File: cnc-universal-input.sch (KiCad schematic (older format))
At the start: 143 parts, among them J1 3PT, J10 2PT, J12 USB_B_Mini, J13 2PT, J14 2PT, J15 2PT, J16 2PT, J17 2PT, J18 2PT, J2 3PT, J3 3PT, J4 3PT, J5 3PT, J6 3PT, J7 3PT, J8 3PT, J9 AVR-ISP-6, Q1 2N7002, Q11 2N7002, Q12 2N7002, Q13 2N7002, Q2 2N7002, Q3 2N7002, Q4 2N7002, Q5 2N7002, Q6 2N7002, Q7 2N7002, Q8 2N7002, Q9 2N7002, SW1 RESET, SW2 BTN, U1 ATmega328PB-AU, U10 EL357NC, U11 EL357NC, U12 EL357NC, U13 EL357NC, U14 EL357NC, U15 EL357NC, U16 EL357NC, U18 CH340G, U19 XL1509-5E1, U2 74HC595, U3 74HC595, U4 74HC595, U5 4051, U6 XL1509-12E1, U7 ADuM1201AR, U8 SGMOP07CXS8G/TR, U9 EL357NC, Y1 16MHz, Y2 12MHz

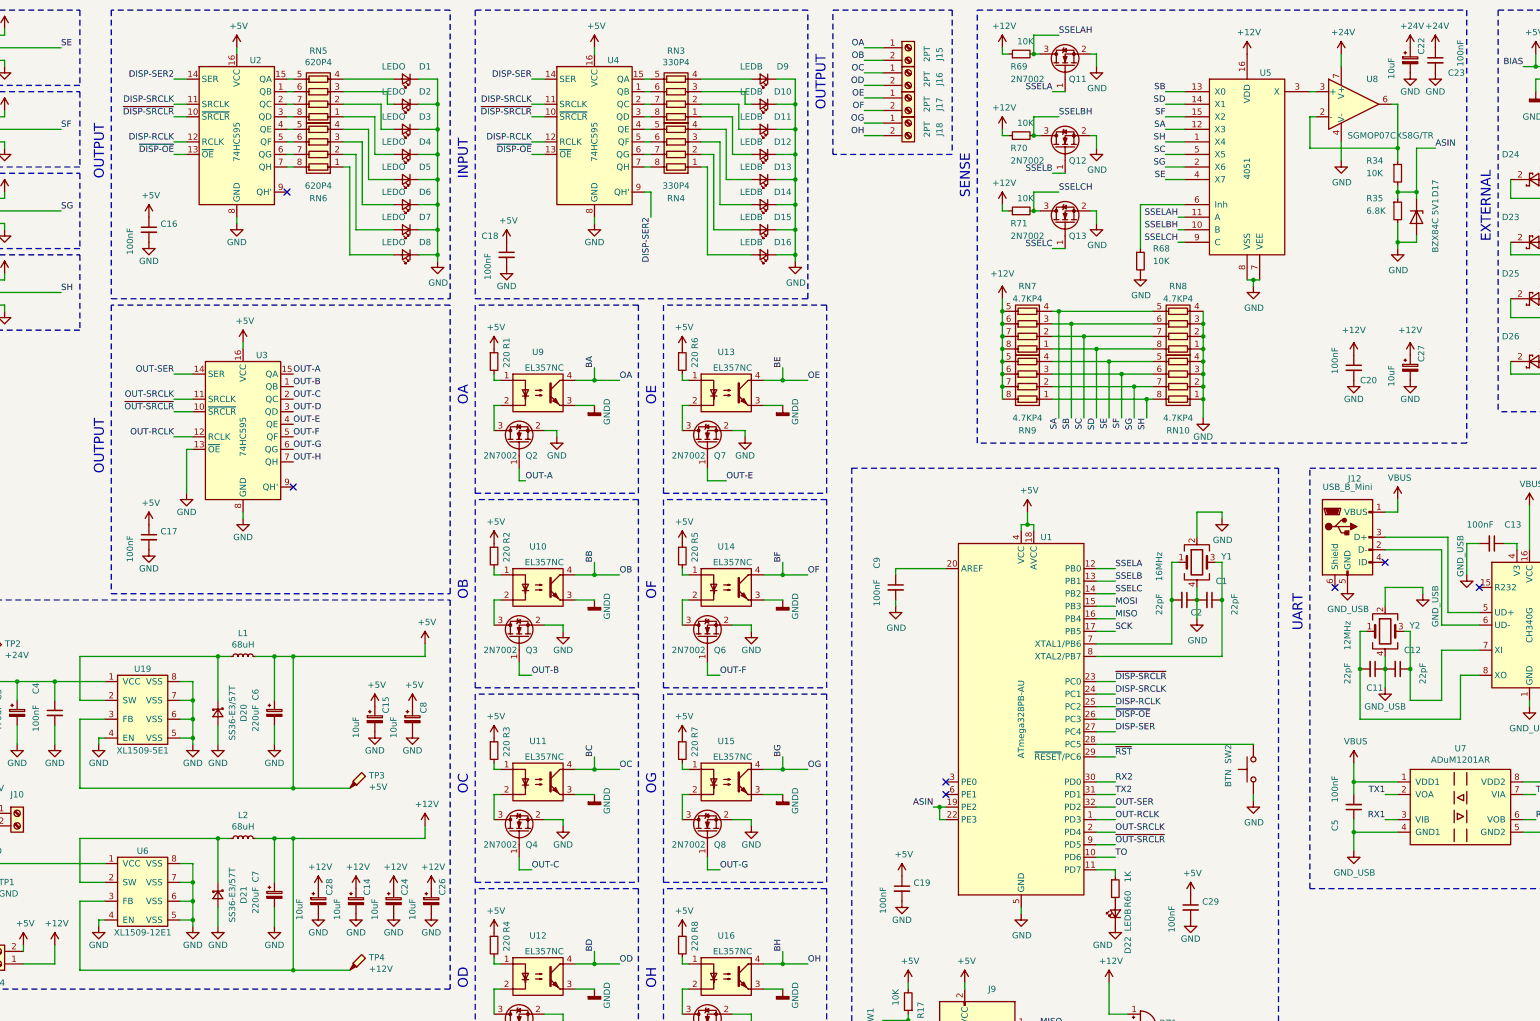
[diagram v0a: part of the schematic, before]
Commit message: Keep something in stock ffs...
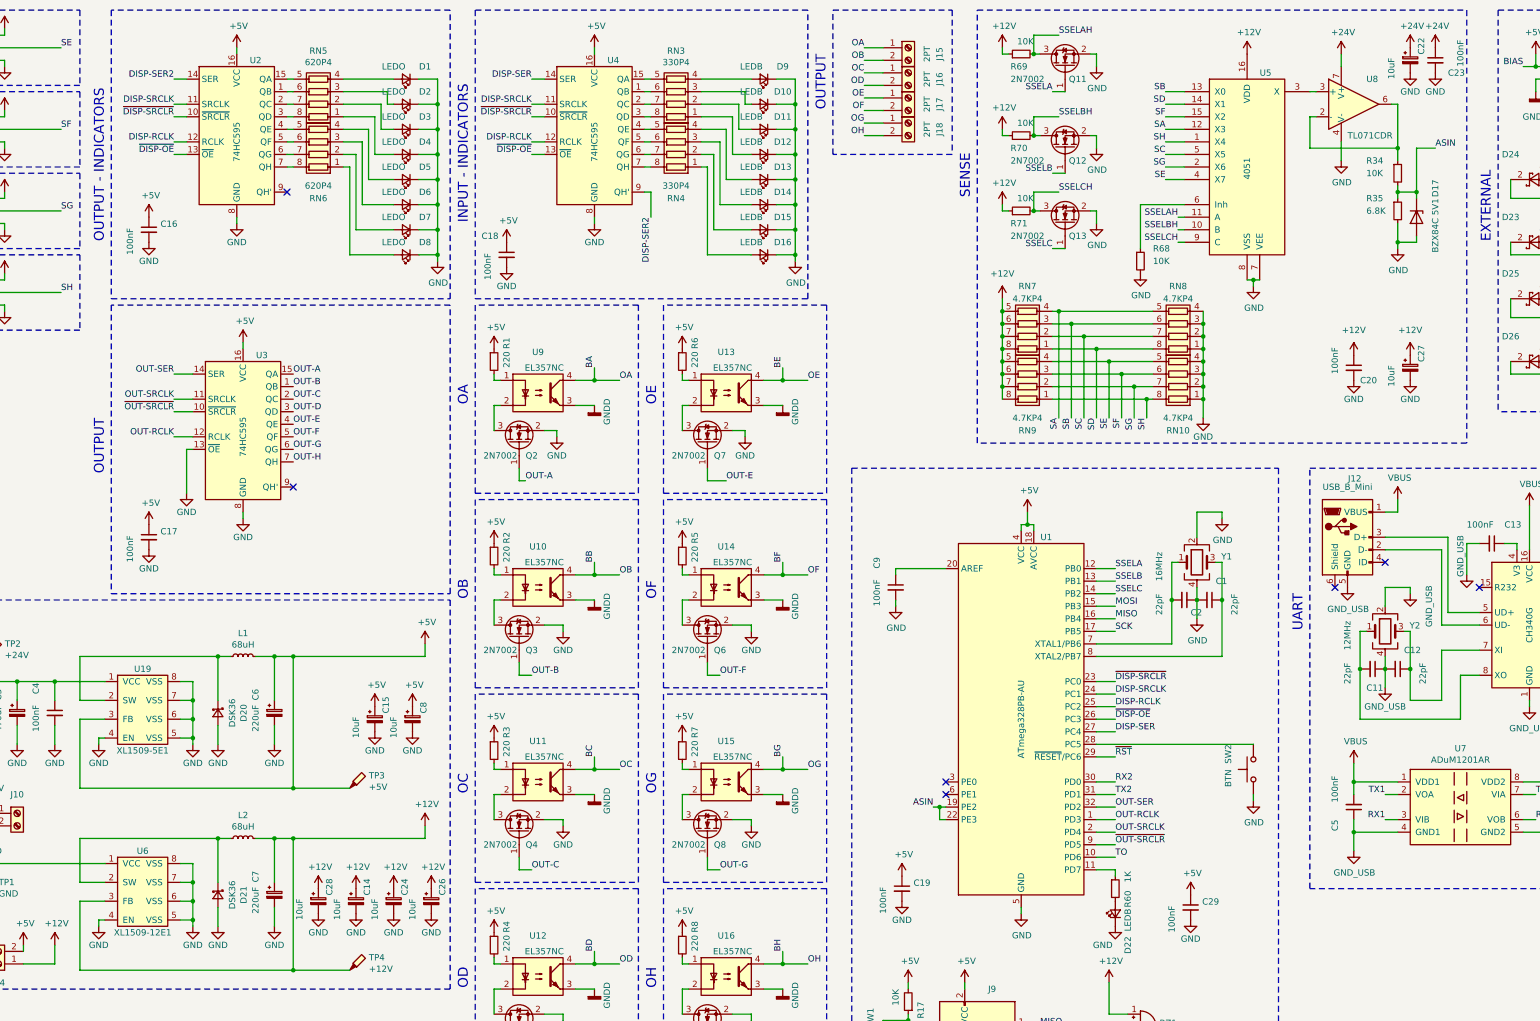
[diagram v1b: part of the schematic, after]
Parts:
- D20, D21: value SS36-E3/57T -> DSK36; footprint Diode_SMD:D_2114_3652Metric -> Diode_SMD:D_SOD-123F; LCSC C35722 -> C106913
- U10, U11, U12, U13, U14, U15, U16, U9: footprint IvyBit-footprints:SOP-4_4.1x4.4x2.54P -> Package_SO:SO-4_4.4x3.9mm_P2.54mm
- U8: value SGMOP07CXS8G/TR -> TL071CDR; LCSC C89712 -> C14449
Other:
- note added: "INPUT - INDICATORS"
- note added: "OUTPUT - INDICATORS"
- note removed: "INPUT"
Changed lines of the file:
@@
 P 13200 1300
 F 0 "U8" H 13300 1500 50  0000 L CNN
-F 1 "SGMOP07CXS8G/TR" H 13150 1050 50  0000 L CNN
+F 1 "TL071CDR" H 13150 1050 50  0000 L CNN
 F 2 "Package_SO:SOIC-8_3.9x4.9mm_P1.27mm" H 13100 1100 50  0001 L CNN
 F 3 "https://datasheet.lcsc.com/lcsc/2004131003_SGMICRO-SGMOP07CXS8G-TR_C89712.pdf" H 13350 1450 50  0001 C CNN
-F 4 "C89712" H 13200 1300 50  0001 C CNN "LCSC"
+F 4 "C14449" H 13200 1300 50  0001 C CNN "LCSC"
 	1    13200 1300
 	1    0    0    -1
@@
 Wire Notes Line
 	8850 550  6200 550
-Text Notes 6150 1900 1    79   ~ 0
-INPUT
+Text Notes 6150 2250 1    79   ~ 0
+INPUT - INDICATORS
 $Comp
 L cnc-universal-input-rescue:LED_Small-Device D1
@@
 Wire Notes Line
 	6000 550  3300 550
-Text Notes 3250 1900 1    79   ~ 0
-OUTPUT
+Text Notes 3250 2400 1    79   ~ 0
+OUTPUT - INDICATORS
 Text Label 11300 5000 0    50   ~ 0
 SSELA
@@
 F 0 "U9" H 6700 3925 50  0000 C CNN
 F 1 "EL357NC" H 6750 3800 50  0000 C CNN
-F 2 "IvyBit-footprints:SOP-4_4.1x4.4x2.54P" H 6500 3400 50  0001 L CIN
+F 2 "Package_SO:SO-4_4.4x3.9mm_P2.54mm" H 6500 3400 50  0001 L CIN
 F 3 "https://datasheet.lcsc.com/lcsc/1810271030_Everlight-Elec-EL357N-C-TA-G_C29981.pdf" H 6700 3600 50  0001 L CNN
 F 4 "C29981" H 6700 3600 50  0001 C CNN "LCSC"
@@
 F 0 "U10" H 6700 5475 50  0000 C CNN
 F 1 "EL357NC" H 6750 5350 50  0000 C CNN
-F 2 "IvyBit-footprints:SOP-4_4.1x4.4x2.54P" H 6500 4950 50  0001 L CIN
+F 2 "Package_SO:SO-4_4.4x3.9mm_P2.54mm" H 6500 4950 50  0001 L CIN
 F 3 "https://datasheet.lcsc.com/lcsc/1810271030_Everlight-Elec-EL357N-C-TA-G_C29981.pdf" H 6700 5150 50  0001 L CNN
 F 4 "C29981" H 6700 5150 50  0001 C CNN "LCSC"
@@
 F 0 "U13" H 8200 3925 50  0000 C CNN
 F 1 "EL357NC" H 8250 3800 50  0000 C CNN
-F 2 "IvyBit-footprints:SOP-4_4.1x4.4x2.54P" H 8000 3400 50  0001 L CIN
+F 2 "Package_SO:SO-4_4.4x3.9mm_P2.54mm" H 8000 3400 50  0001 L CIN
 F 3 "https://datasheet.lcsc.com/lcsc/1810271030_Everlight-Elec-EL357N-C-TA-G_C29981.pdf" H 8200 3600 50  0001 L CNN
 F 4 "C29981" H 8200 3600 50  0001 C CNN "LCSC"
@@
 P 4150 6150
 F 0 "D20" H 4150 6355 50  0000 C CNN
-F 1 "SS36-E3/57T" H 4150 6264 50  0000 C CNN
-F 2 "Diode_SMD:D_2114_3652Metric" V 4150 6150 50  0001 C CNN
-F 3 "https://datasheet.lcsc.com/lcsc/1809042323_Vishay-Intertech-SS36-E3-57T_C35722.pdf" V 4150 6150 50  0001 C CNN
-F 4 "C35722" H 4150 6150 50  0001 C CNN "LCSC"
+F 1 "DSK36" H 4150 6264 50  0000 C CNN
+F 2 "Diode_SMD:D_SOD-123F" V 4150 6150 50  0001 C CNN
+F 3 "https://datasheet.lcsc.com/lcsc/1809301213_MDD%EF%BC%88Microdiode-Electronics%EF%BC%89-DSK36_C106913.pdf" V 4150 6150 50  0001 C CNN
+F 4 "C106913" H 4150 6150 50  0001 C CNN "LCSC"
 	1    4150 6150
 	0    1    1    0
@@
 	13650 5800 13650 5500
 Wire Wire Line
-	13750 5200 13750 5150
+	13650 5200 13650 5150
 Wire Wire Line
-	13750 5150 13450 5150
+	13650 5150 13450 5150
 Wire Wire Line
 	13450 5150 13450 5300
@@
 L cnc-universal-input-rescue:GND_USB-IvyBit #PWR0145
 U 1 1 6211F579
-P 13750 5200
-F 0 "#PWR0145" H 13750 4950 50  0001 C CNN
-F 1 "GND_USB" V 13850 5100 50  0000 C CNN
-F 2 "" H 13750 5200 50  0001 C CNN
-F 3 "" H 13750 5200 50  0001 C CNN
-	1    13750 5200
+P 13650 5200
+F 0 "#PWR0145" H 13650 4950 50  0001 C CNN
+F 1 "GND_USB" V 13800 5100 50  0000 C CNN
+F 2 "" H 13650 5200 50  0001 C CNN
+F 3 "" H 13650 5200 50  0001 C CNN
+	1    13650 5200
 	1    0    0    -1
 $EndComp
@@
 P 4150 7600
 F 0 "D21" H 4150 7805 50  0000 C CNN
-F 1 "SS36-E3/57T" H 4150 7714 50  0000 C CNN
-F 2 "Diode_SMD:D_2114_3652Metric" V 4150 7600 50  0001 C CNN
-F 3 "https://datasheet.lcsc.com/lcsc/1809042323_Vishay-Intertech-SS36-E3-57T_C35722.pdf" V 4150 7600 50  0001 C CNN
-F 4 "C35722" H 4150 7600 50  0001 C CNN "LCSC"
+F 1 "DSK36" H 4150 7714 50  0000 C CNN
+F 2 "Diode_SMD:D_SOD-123F" V 4150 7600 50  0001 C CNN
+F 3 "https://datasheet.lcsc.com/lcsc/1809301213_MDD%EF%BC%88Microdiode-Electronics%EF%BC%89-DSK36_C106913.pdf" V 4150 7600 50  0001 C CNN
+F 4 "C106913" H 4150 7600 50  0001 C CNN "LCSC"
 	1    4150 7600
 	0    1    1    0
@@
 F 0 "U11" H 6700 7025 50  0000 C CNN
 F 1 "EL357NC" H 6750 6900 50  0000 C CNN
-F 2 "IvyBit-footprints:SOP-4_4.1x4.4x2.54P" H 6500 6500 50  0001 L CIN
+F 2 "Package_SO:SO-4_4.4x3.9mm_P2.54mm" H 6500 6500 50  0001 L CIN
 F 3 "https://datasheet.lcsc.com/lcsc/1810271030_Everlight-Elec-EL357N-C-TA-G_C29981.pdf" H 6700 6700 50  0001 L CNN
 F 4 "C29981" H 6700 6700 50  0001 C CNN "LCSC"
@@
 F 0 "U12" H 6700 8575 50  0000 C CNN
 F 1 "EL357NC" H 6750 8450 50  0000 C CNN
-F 2 "IvyBit-footprints:SOP-4_4.1x4.4x2.54P" H 6500 8050 50  0001 L CIN
+F 2 "Package_SO:SO-4_4.4x3.9mm_P2.54mm" H 6500 8050 50  0001 L CIN
 F 3 "https://datasheet.lcsc.com/lcsc/1810271030_Everlight-Elec-EL357N-C-TA-G_C29981.pdf" H 6700 8250 50  0001 L CNN
 F 4 "C29981" H 6700 8250 50  0001 C CNN "LCSC"
@@
 F 0 "U14" H 8200 5475 50  0000 C CNN
 F 1 "EL357NC" H 8250 5350 50  0000 C CNN
-F 2 "IvyBit-footprints:SOP-4_4.1x4.4x2.54P" H 8000 4950 50  0001 L CIN
+F 2 "Package_SO:SO-4_4.4x3.9mm_P2.54mm" H 8000 4950 50  0001 L CIN
 F 3 "https://datasheet.lcsc.com/lcsc/1810271030_Everlight-Elec-EL357N-C-TA-G_C29981.pdf" H 8200 5150 50  0001 L CNN
 F 4 "C29981" H 8200 5150 50  0001 C CNN "LCSC"
@@
 F 0 "U15" H 8200 7025 50  0000 C CNN
 F 1 "EL357NC" H 8250 6900 50  0000 C CNN
-F 2 "IvyBit-footprints:SOP-4_4.1x4.4x2.54P" H 8000 6500 50  0001 L CIN
+F 2 "Package_SO:SO-4_4.4x3.9mm_P2.54mm" H 8000 6500 50  0001 L CIN
 F 3 "https://datasheet.lcsc.com/lcsc/1810271030_Everlight-Elec-EL357N-C-TA-G_C29981.pdf" H 8200 6700 50  0001 L CNN
 F 4 "C29981" H 8200 6700 50  0001 C CNN "LCSC"
@@
 F 0 "U16" H 8200 8575 50  0000 C CNN
 F 1 "EL357NC" H 8250 8450 50  0000 C CNN
-F 2 "IvyBit-footprints:SOP-4_4.1x4.4x2.54P" H 8000 8050 50  0001 L CIN
+F 2 "Package_SO:SO-4_4.4x3.9mm_P2.54mm" H 8000 8050 50  0001 L CIN
 F 3 "https://datasheet.lcsc.com/lcsc/1810271030_Everlight-Elec-EL357N-C-TA-G_C29981.pdf" H 8200 8250 50  0001 L CNN
 F 4 "C29981" H 8200 8250 50  0001 C CNN "LCSC"

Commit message: switched the 5ohm resistors with 10k ones... burn baby burn
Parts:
- R17, R34, R68, R69, R70, R71: LCSC C17724 -> C17414
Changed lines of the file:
@@
 F 1 "10K" H 13300 1850 50  0000 L CNN
 F 2 "Resistor_SMD:R_0805_2012Metric" H 13550 1850 50  0001 C CNN
-F 3 "https://datasheet.lcsc.com/lcsc/1810301816_UNI-ROYAL-Uniroyal-Elec-0805W8F510KT5E_C17724.pdf" H 13550 1850 50  0001 C CNN
-F 4 "C17724" H 13550 1850 50  0001 C CNN "LCSC"
+F 3 "https://datasheet.lcsc.com/lcsc/2110251730_UNI-ROYAL-Uniroyal-Elec-0805W8F1002T5E_C17414.pdf" H 13550 1850 50  0001 C CNN
+F 4 "C17414" H 13550 1850 50  0001 C CNN "LCSC"
 	1    13550 1850
 	1    0    0    -1
@@
 F 1 "10K" V 9750 8350 50  0000 L CNN
 F 2 "Resistor_SMD:R_0805_2012Metric" H 9650 8450 50  0001 C CNN
-F 3 "https://datasheet.lcsc.com/lcsc/1810301816_UNI-ROYAL-Uniroyal-Elec-0805W8F510KT5E_C17724.pdf" H 9650 8450 50  0001 C CNN
-F 4 "C17724" H 9650 8450 50  0001 C CNN "LCSC"
+F 3 "https://datasheet.lcsc.com/lcsc/2110251730_UNI-ROYAL-Uniroyal-Elec-0805W8F1002T5E_C17414.pdf" H 9650 8450 50  0001 C CNN
+F 4 "C17414" H 9650 8450 50  0001 C CNN "LCSC"
 	1    9650 8450
 	-1   0    0    1
@@
 F 1 "10K" H 11600 2550 50  0000 L CNN
 F 2 "Resistor_SMD:R_0805_2012Metric" H 11500 2550 50  0001 C CNN
-F 3 "https://datasheet.lcsc.com/lcsc/1810301816_UNI-ROYAL-Uniroyal-Elec-0805W8F510KT5E_C17724.pdf" H 11500 2550 50  0001 C CNN
-F 4 "C17724" H 11500 2550 50  0001 C CNN "LCSC"
+F 3 "https://datasheet.lcsc.com/lcsc/2110251730_UNI-ROYAL-Uniroyal-Elec-0805W8F1002T5E_C17414.pdf" H 11500 2550 50  0001 C CNN
+F 4 "C17414" H 11500 2550 50  0001 C CNN "LCSC"
 	1    11500 2550
 	1    0    0    -1
@@
 F 1 "10K" V 10650 800 50  0000 L CNN
 F 2 "Resistor_SMD:R_0805_2012Metric" H 10550 900 50  0001 C CNN
-F 3 "https://datasheet.lcsc.com/lcsc/1810301816_UNI-ROYAL-Uniroyal-Elec-0805W8F510KT5E_C17724.pdf" H 10550 900 50  0001 C CNN
-F 4 "C17724" H 10550 900 50  0001 C CNN "LCSC"
+F 3 "https://datasheet.lcsc.com/lcsc/2110251730_UNI-ROYAL-Uniroyal-Elec-0805W8F1002T5E_C17414.pdf" H 10550 900 50  0001 C CNN
+F 4 "C17414" H 10550 900 50  0001 C CNN "LCSC"
 	1    10550 900
 	0    -1   -1   0
@@
 F 1 "10K" V 10650 1450 50  0000 L CNN
 F 2 "Resistor_SMD:R_0805_2012Metric" H 10550 1550 50  0001 C CNN
-F 3 "https://datasheet.lcsc.com/lcsc/1810301816_UNI-ROYAL-Uniroyal-Elec-0805W8F510KT5E_C17724.pdf" H 10550 1550 50  0001 C CNN
-F 4 "C17724" H 10550 1550 50  0001 C CNN "LCSC"
+F 3 "https://datasheet.lcsc.com/lcsc/2110251730_UNI-ROYAL-Uniroyal-Elec-0805W8F1002T5E_C17414.pdf" H 10550 1550 50  0001 C CNN
+F 4 "C17414" H 10550 1550 50  0001 C CNN "LCSC"
 	1    10550 1550
 	0    -1   -1   0
@@
 F 1 "10K" V 10650 2050 50  0000 L CNN
 F 2 "Resistor_SMD:R_0805_2012Metric" H 10550 2150 50  0001 C CNN
-F 3 "https://datasheet.lcsc.com/lcsc/1810301816_UNI-ROYAL-Uniroyal-Elec-0805W8F510KT5E_C17724.pdf" H 10550 2150 50  0001 C CNN
-F 4 "C17724" H 10550 2150 50  0001 C CNN "LCSC"
+F 3 "https://datasheet.lcsc.com/lcsc/2110251730_UNI-ROYAL-Uniroyal-Elec-0805W8F1002T5E_C17414.pdf" H 10550 2150 50  0001 C CNN
+F 4 "C17414" H 10550 2150 50  0001 C CNN "LCSC"
 	1    10550 2150
 	0    -1   -1   0

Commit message: wrong opamp...
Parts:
- U8: LCSC C14449 -> C89712
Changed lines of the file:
@@
 Wire Wire Line
 	1150 950  1150 1000
-$Comp
-L cnc-universal-input-rescue:AD8001AR-Amplifier_Operational U8
-U 1 1 5FEB57AA
-P 13200 1300
-F 0 "U8" H 13300 1500 50  0000 L CNN
-F 1 "TL071CDR" H 13150 1050 50  0000 L CNN
-F 2 "Package_SO:SOIC-8_3.9x4.9mm_P1.27mm" H 13100 1100 50  0001 L CNN
-F 3 "https://datasheet.lcsc.com/lcsc/2004131003_SGMICRO-SGMOP07CXS8G-TR_C89712.pdf" H 13350 1450 50  0001 C CNN
-F 4 "C14449" H 13200 1300 50  0001 C CNN "LCSC"
-	1    13200 1300
-	1    0    0    -1
-$EndComp
 Wire Wire Line
 	13100 1600 13100 1750
@@
 $EndComp
 NoConn ~ 13050 5150
+$Comp
+L cnc-universal-input-rescue:AD8001AR-Amplifier_Operational U8
+U 1 1 5FEB57AA
+P 13200 1300
+F 0 "U8" H 13300 1500 50  0000 L CNN
+F 1 "TL071CDR" H 13150 1050 50  0000 L CNN
+F 2 "Package_SO:SOIC-8_3.9x4.9mm_P1.27mm" H 13100 1100 50  0001 L CNN
+F 3 "https://datasheet.lcsc.com/lcsc/2004131003_SGMICRO-SGMOP07CXS8G-TR_C89712.pdf" H 13350 1450 50  0001 C CNN
+F 4 "C89712" H 13200 1300 50  0001 C CNN "LCSC"
+	1    13200 1300
+	1    0    0    -1
+$EndComp
 $EndSCHEMATC

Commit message: We wait for no buzzers
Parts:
- U8: LCSC C89712 -> C14449
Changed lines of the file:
@@
 F 2 "Package_SO:SOIC-8_3.9x4.9mm_P1.27mm" H 13100 1100 50  0001 L CNN
 F 3 "https://datasheet.lcsc.com/lcsc/2004131003_SGMICRO-SGMOP07CXS8G-TR_C89712.pdf" H 13350 1450 50  0001 C CNN
-F 4 "C89712" H 13200 1300 50  0001 C CNN "LCSC"
+F 4 "C14449" H 13200 1300 50  0001 C CNN "LCSC"
 	1    13200 1300
 	1    0    0    -1
